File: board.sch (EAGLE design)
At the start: 89 parts, among them J1 AVR_SPI_PRG_6NS, U1 TPS2112A, U2 MAX1555, U3 USD-SOCKETNEW, U4 3.3V, U5 2.8V, U6 74HC595, Y1 8MHz, Y2 12.288MHz

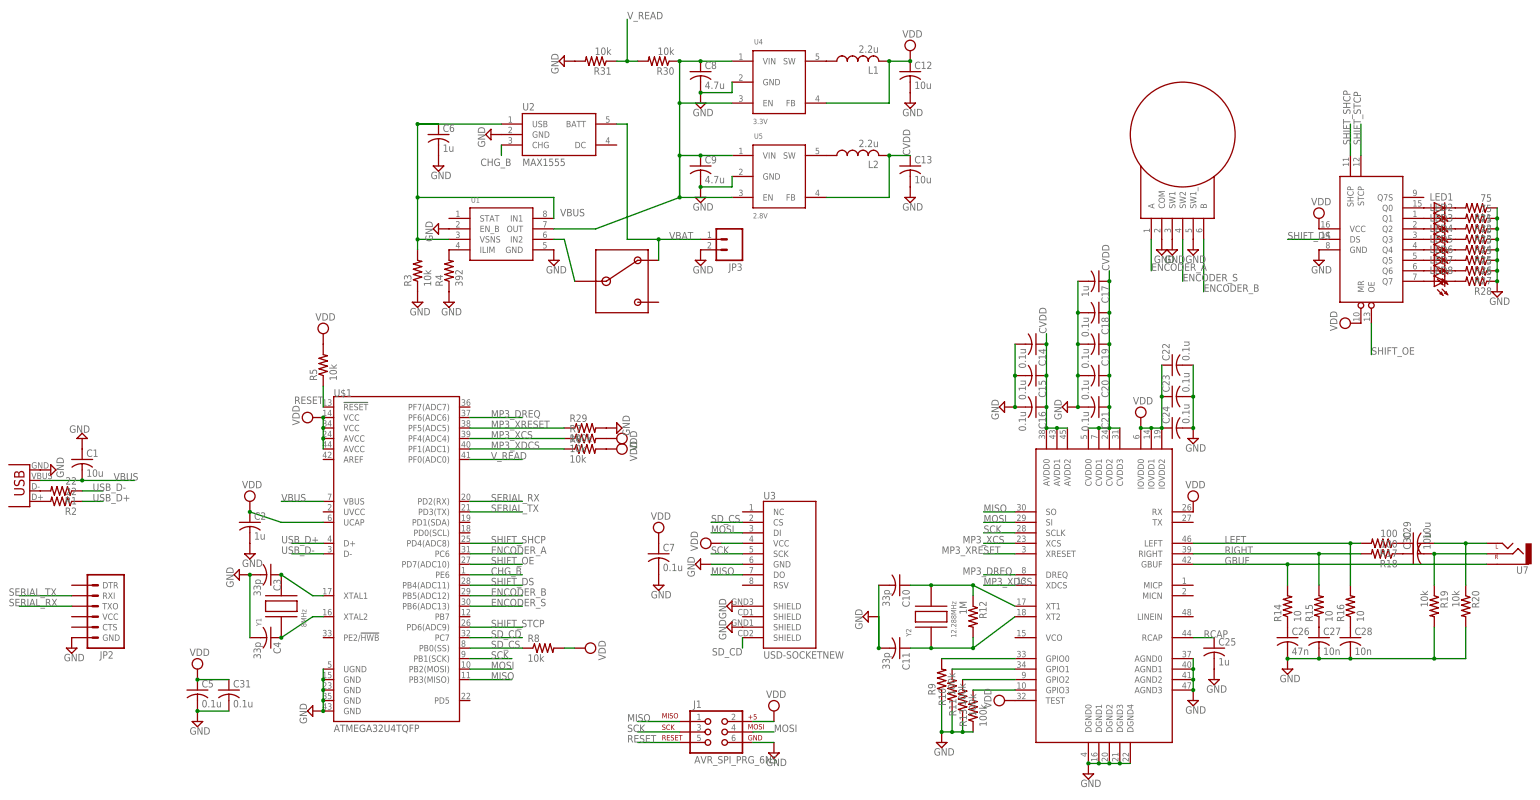
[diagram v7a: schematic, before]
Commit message: Re-ordered components, added identifiers to BOM, and fixed power switching
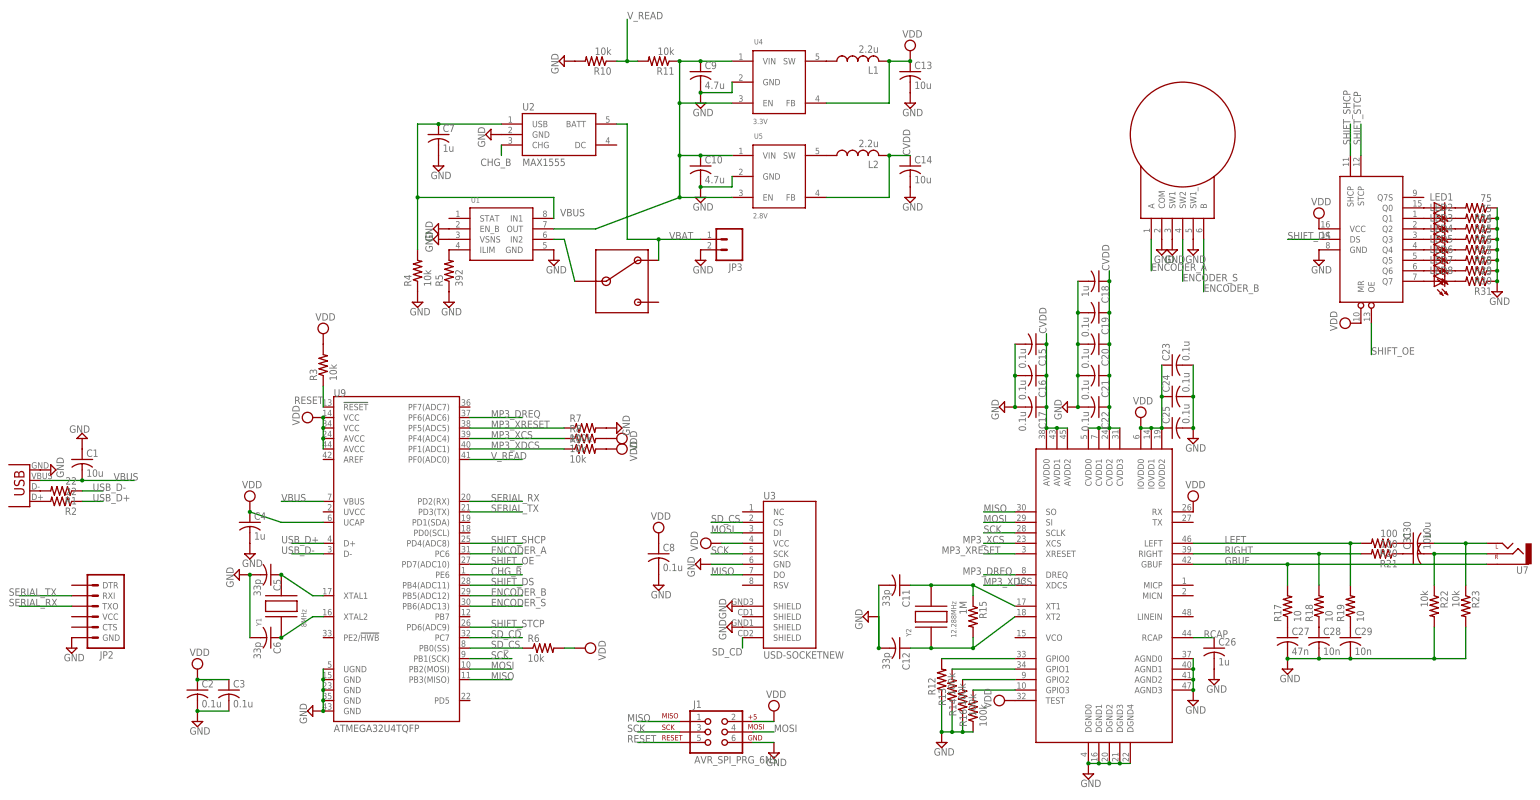
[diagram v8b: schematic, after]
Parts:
- C10: value 33p -> 4.7u
- C12: value 10u -> 33p
- C14, C31: value 0.1u -> 10u
- C17, C2, C25: value 1u -> 0.1u
- C18, C7: value 0.1u -> 1u
- C26: value 47n -> 1u
- C27: value 10n -> 47n
- C29: value 10u -> 10n
- C3: value 33p -> 0.1u
- C4: value 33p -> 1u
- C5: value 0.1u -> 33p
- C6: value 1u -> 33p
- C8: value 4.7u -> 0.1u
- R10, R11: value 100k -> 10k; device rcl:R-US_R0603W -> rcl:R-US_R0603
- R12: value 1M -> 100k; device rcl:R-US_R0603 -> rcl:R-US_R0603W
- R14, R16: value 10 -> 100k
- R15: value 10 -> 1M; device rcl:R-US_R0603W -> rcl:R-US_R0603
- R17, R18: value 100 -> 10
- R19: value 10k -> 10
- R20: value 10k -> 100
- R21: value 75 -> 100
- R22, R23: value 75 -> 10k
- R29: value 100k -> 75
- R30, R31: value 10k -> 75; device rcl:R-US_R0603 -> rcl:R-US_R0603W
- R4: value 392 -> 10k
- R5: value 10k -> 392
- R7: value 10k -> 100k
- R9: value 100k -> 10k
- renumbered U$1 to U9, U$2 to U8
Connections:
- net CVDD: now also C22.1; no longer C13.1
- net GBUF: now also R17.2; no longer R14.2
- net GND: now also C29.2, R10.2, R12.1, R14.1, R16.1, R22.2, R23.2, R29.1, R30.1, R31.1, R5.1, R7.2, U1.VSNS; no longer C31.2, R10.1, R11.1, R19.2, R20.2, R21.1, R22.1, R23.1, R29.2, R3.1, R31.2, R9.1
- net GPIO0: now also R12.2; no longer R9.2
- net GPIO1: now also R13.2; no longer R10.2
- net GPIO2: now also R14.2; no longer R11.2
- net GPIO3: now also R16.2; no longer R13.2
- net LEFT: now also R19.2, R20.2; no longer R16.2, R17.2
- net MP3_XCS: now also R8.1; no longer R7.1
- net MP3_XDCS: now also R9.1; no longer R6.1
- net MP3_XRESET: now also R7.1; no longer R29.1
- net N$10: now also C31.1, R21.1; no longer C30.1, R18.1
- net N$11: now also C30.1, R20.1; no longer C29.1, R17.1
- net N$12: now also C31.2, R22.1; no longer C30.2, R19.1
- net N$13: now also C30.2, R23.1; no longer C29.2, R20.1
- net N$14: now also C6.1; no longer C4.1
- net N$17: now also R5.2; no longer R4.2
- net N$18: now also C10.1, R11.1; no longer C8.1, R30.1
- net N$2: now also C5.1; no longer C3.1
- net N$27: now also R24.2; no longer R21.2
- net N$28: now also R25.2; no longer R22.2
- net N$29: now also R26.2; no longer R23.2
- net N$3: now also C27.1, R17.1; no longer C26.1, R14.1
- net N$30: now also R27.2; no longer R24.2
- net N$31: now also R28.2; no longer R25.2
- net N$32: now also R29.2; no longer R26.2
- net N$33: now also R30.2; no longer R27.2
- net N$34: now also R31.2; no longer R28.2
- net N$4: now also C28.1, R18.1; no longer C27.1, R15.1
- net N$5: now also C29.1, R19.1; no longer C28.1, R16.1
- net N$7: now also C12.1, R15.2; no longer C11.1, R12.2
- net N$8: now also C11.1, R15.1; no longer C10.1, R12.1
- net RCAP: now also C26.1; no longer C25.1
- net RESET: now also R3.1; no longer R5.1
- net RIGHT: now also R21.2; no longer R15.2
- net SD_CS: now also R6.1; no longer R8.1
- net VBUS: now also C7.1, R4.2; no longer C6.1, R3.2, U1.VSNS
- net VDD: now also C13.1, C25.1, C3.1, C4.1, C8.1, R3.2, R9.2; no longer C12.1, C22.1, C31.1, C5.1, C7.1, R5.2, R7.2
- net V_READ: now also R10.1, R11.2; no longer R30.2, R31.1
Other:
- moved on the sheet: C10, C11, C12, C13, C14, C15, C16, C17, C18, C19, C2, C20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
